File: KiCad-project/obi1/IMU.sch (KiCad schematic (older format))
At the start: 6 parts, among them U6 BMF055

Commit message: Routear
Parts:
- added C42: @1uF;6.3V;X5R;0805;10%, Capacitor_SMD:C_0805_2012Metric_Pad1.18x1.45mm_HandSolder, symbol Device:C
- added R19: @20;1/4W;0805;1%, Resistor_SMD:R_0805_2012Metric_Pad1.20x1.40mm_HandSolder, symbol Device:R
- renumbered C42 to C43, C43 to C44, C44 to C45, R19 to R20
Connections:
- net +3V3: now also C42.1, R19.1
- net GND: now also C42.2
- new net nReset: R19.2
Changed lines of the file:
@@
 	4450 6300 4450 6550
 Wire Wire Line
-	2100 6550 3950 6550
+	2100 6550 2500 6550
 Connection ~ 4250 6550
 Wire Wire Line
 	4250 6550 4350 6550
-Text GLabel 2950 4700 0    50   Input ~ 0
+Text GLabel 2400 4600 0    50   Input ~ 0
 nReset
 $Comp
-L Device:C C42
+L Device:C C43
 U 1 1 605F8DE4
 P 3050 5000
-F 0 "C42" H 3165 5046 50  0000 L CNN
+F 0 "C43" H 3165 5046 50  0000 L CNN
 F 1 "@1uF;6.3V;X5R;0805;10%" H 2550 4900 50  0000 L CNN
 F 2 "Capacitor_SMD:C_0805_2012Metric_Pad1.18x1.45mm_HandSolder" H 3088 4850 50  0001 C CNN
@@
 $EndComp
 Wire Wire Line
-	3550 4800 3050 4800
-Wire Wire Line
 	3050 4800 3050 4850
 Wire Wire Line
@@
 	4350 6550 4450 6550
 $Comp
-L Device:R R19
+L Device:R R20
 U 1 1 605FCDD0
 P 3200 4700
-F 0 "R19" V 2993 4700 50  0000 C CNN
+F 0 "R20" V 2993 4700 50  0000 C CNN
 F 1 "@10K;1/4W;0805;1%" V 3100 4700 50  0000 C CNN
 F 2 "Resistor_SMD:R_0805_2012Metric_Pad1.20x1.40mm_HandSolder" V 3130 4700 50  0001 C CNN
@@
 $EndComp
 Wire Wire Line
-	3350 4700 3550 4700
-Wire Wire Line
 	3050 4700 3000 4700
 Connection ~ 3000 4700
-Wire Wire Line
-	3000 4700 2950 4700
-$Comp
-L Device:C C44
+$Comp
+L Device:C C45
 U 1 1 605FF628
 P 5650 4400
-F 0 "C44" H 5765 4446 50  0000 L CNN
+F 0 "C45" H 5765 4446 50  0000 L CNN
 F 1 "@6800pF;10V;X7R;0603;10%" H 5765 4355 50  0000 L CNN
 F 2 "Capacitor_SMD:C_0603_1608Metric_Pad1.08x0.95mm_HandSolder" H 5688 4250 50  0001 C CNN
@@
 Connection ~ 4450 6550
 $Comp
-L Device:C C43
+L Device:C C44
 U 1 1 606014E1
 P 5200 4400
-F 0 "C43" H 5315 4446 50  0000 L CNN
+F 0 "C44" H 5315 4446 50  0000 L CNN
 F 1 "@0.12uF;10V;X7R;0603;10%" H 4750 4500 50  0000 L CNN
 F 2 "Capacitor_SMD:C_0603_1608Metric_Pad1.08x0.95mm_HandSolder" H 5238 4250 50  0001 C CNN
@@
 	3950 6550 3950 6750
 Connection ~ 3950 6550
-Wire Wire Line
-	3950 6550 4250 6550
+$Comp
+L Device:C C42
+U 1 1 60648C09
+P 2350 5500
+F 0 "C42" H 2465 5546 50  0000 L CNN
+F 1 "@1uF;6.3V;X5R;0805;10%" H 1850 5400 50  0000 L CNN
+F 2 "Capacitor_SMD:C_0805_2012Metric_Pad1.18x1.45mm_HandSolder" H 2388 5350 50  0001 C CNN
+F 3 "~" H 2350 5500 50  0001 C CNN
+	1    2350 5500
+	1    0    0    -1
+$EndComp
+Wire Wire Line
+	2500 6550 2500 5650
+Wire Wire Line
+	2500 5650 2350 5650
+Connection ~ 2500 6550
+Wire Wire Line
+	2500 6550 3950 6550
+Wire Wire Line
+	3550 4800 3050 4800
+Wire Wire Line
+	3350 4700 3550 4700
+$Comp
+L Device:R R19
+U 1 1 60650B61
+P 2600 4600
+F 0 "R19" V 2393 4600 50  0000 C CNN
+F 1 "@20;1/4W;0805;1%" V 2500 4600 50  0000 C CNN
+F 2 "Resistor_SMD:R_0805_2012Metric_Pad1.20x1.40mm_HandSolder" V 2530 4600 50  0001 C CNN
+F 3 "~" H 2600 4600 50  0001 C CNN
+	1    2600 4600
+	0    1    1    0
+$EndComp
+Wire Wire Line
+	2450 4600 2400 4600
+Wire Wire Line
+	2750 4600 2750 4700
+Wire Wire Line
+	2750 5350 2350 5350
+Wire Wire Line
+	2750 4700 3000 4700
+Connection ~ 2750 4700
+Wire Wire Line
+	2750 4700 2750 5350
 $EndSCHEMATC

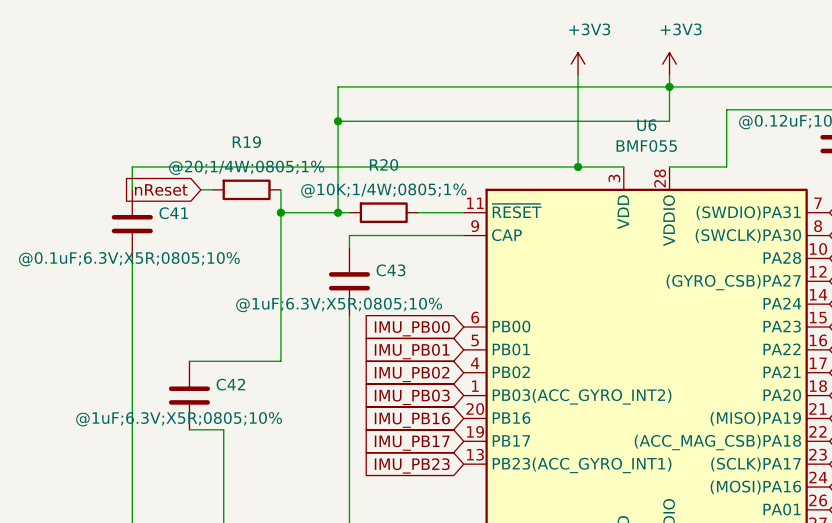
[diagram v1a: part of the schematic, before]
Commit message: Resize board, change layout, re-route IO pins, new imu added
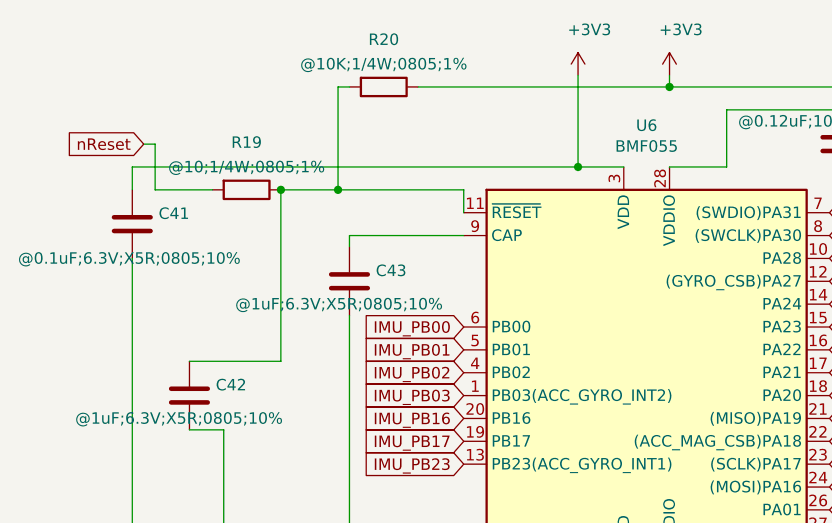
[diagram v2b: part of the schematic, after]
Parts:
- R19: value @20;1/4W;0805;1% -> @10;1/4W;0805;1%
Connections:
- net +3V3: now also R20.1; no longer C42.1, R19.1, R20.2
- net at U6.11 (~RESET): now also C42.1, R19.1, R20.2; no longer R20.1
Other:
- moved on the sheet: R20
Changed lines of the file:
@@
 Wire Wire Line
 	4250 6550 4350 6550
-Text GLabel 2400 4600 0    50   Input ~ 0
+Text GLabel 2150 4400 0    50   Input ~ 0
 nReset
 $Comp
@@
 L Device:R R20
 U 1 1 605FCDD0
-P 3200 4700
-F 0 "R20" V 2993 4700 50  0000 C CNN
-F 1 "@10K;1/4W;0805;1%" V 3100 4700 50  0000 C CNN
-F 2 "Resistor_SMD:R_0805_2012Metric_Pad1.20x1.40mm_HandSolder" V 3130 4700 50  0001 C CNN
-F 3 "~" H 3200 4700 50  0001 C CNN
-	1    3200 4700
+P 3200 4150
+F 0 "R20" V 2993 4150 50  0000 C CNN
+F 1 "@10K;1/4W;0805;1%" V 3100 4150 50  0000 C CNN
+F 2 "Resistor_SMD:R_0805_2012Metric_Pad1.20x1.40mm_HandSolder" V 3130 4150 50  0001 C CNN
+F 3 "~" H 3200 4150 50  0001 C CNN
+	1    3200 4150
 	0    1    1    0
 $EndComp
-Wire Wire Line
-	3050 4700 3000 4700
-Connection ~ 3000 4700
 $Comp
 L Device:C C45
@@
 Connection ~ 5650 4250
 Wire Wire Line
-	4450 4150 3000 4150
+	4450 4150 3350 4150
 Connection ~ 4450 4150
-Wire Wire Line
-	3000 4150 3000 4300
-Wire Wire Line
-	3000 4300 3000 4700
-Connection ~ 3000 4300
-Wire Wire Line
-	4450 4300 3000 4300
-Wire Wire Line
-	4450 4300 4450 4150
 Wire Wire Line
 	4450 4500 4700 4500
@@
 Wire Wire Line
 	3550 4800 3050 4800
-Wire Wire Line
-	3350 4700 3550 4700
 $Comp
 L Device:R R19
@@
 P 2600 4600
 F 0 "R19" V 2393 4600 50  0000 C CNN
-F 1 "@20;1/4W;0805;1%" V 2500 4600 50  0000 C CNN
+F 1 "@10;1/4W;0805;1%" V 2500 4600 50  0000 C CNN
 F 2 "Resistor_SMD:R_0805_2012Metric_Pad1.20x1.40mm_HandSolder" V 2530 4600 50  0001 C CNN
 F 3 "~" H 2600 4600 50  0001 C CNN
@@
 $EndComp
 Wire Wire Line
-	2450 4600 2400 4600
-Wire Wire Line
-	2750 4600 2750 4700
-Wire Wire Line
 	2750 5350 2350 5350
 Wire Wire Line
-	2750 4700 3000 4700
-Connection ~ 2750 4700
+	2200 4600 2200 4400
 Wire Wire Line
-	2750 4700 2750 5350
+	2200 4400 2150 4400
+Wire Wire Line
+	2200 4600 2450 4600
+Wire Wire Line
+	3050 4150 3000 4150
+Wire Wire Line
+	2750 4600 2750 5350
+Wire Wire Line
+	3550 4600 3550 4700
+Connection ~ 2750 4600
+Wire Wire Line
+	3000 4150 3000 4600
+Wire Wire Line
+	2750 4600 3000 4600
+Connection ~ 3000 4600
+Wire Wire Line
+	3000 4600 3550 4600
 $EndSCHEMATC

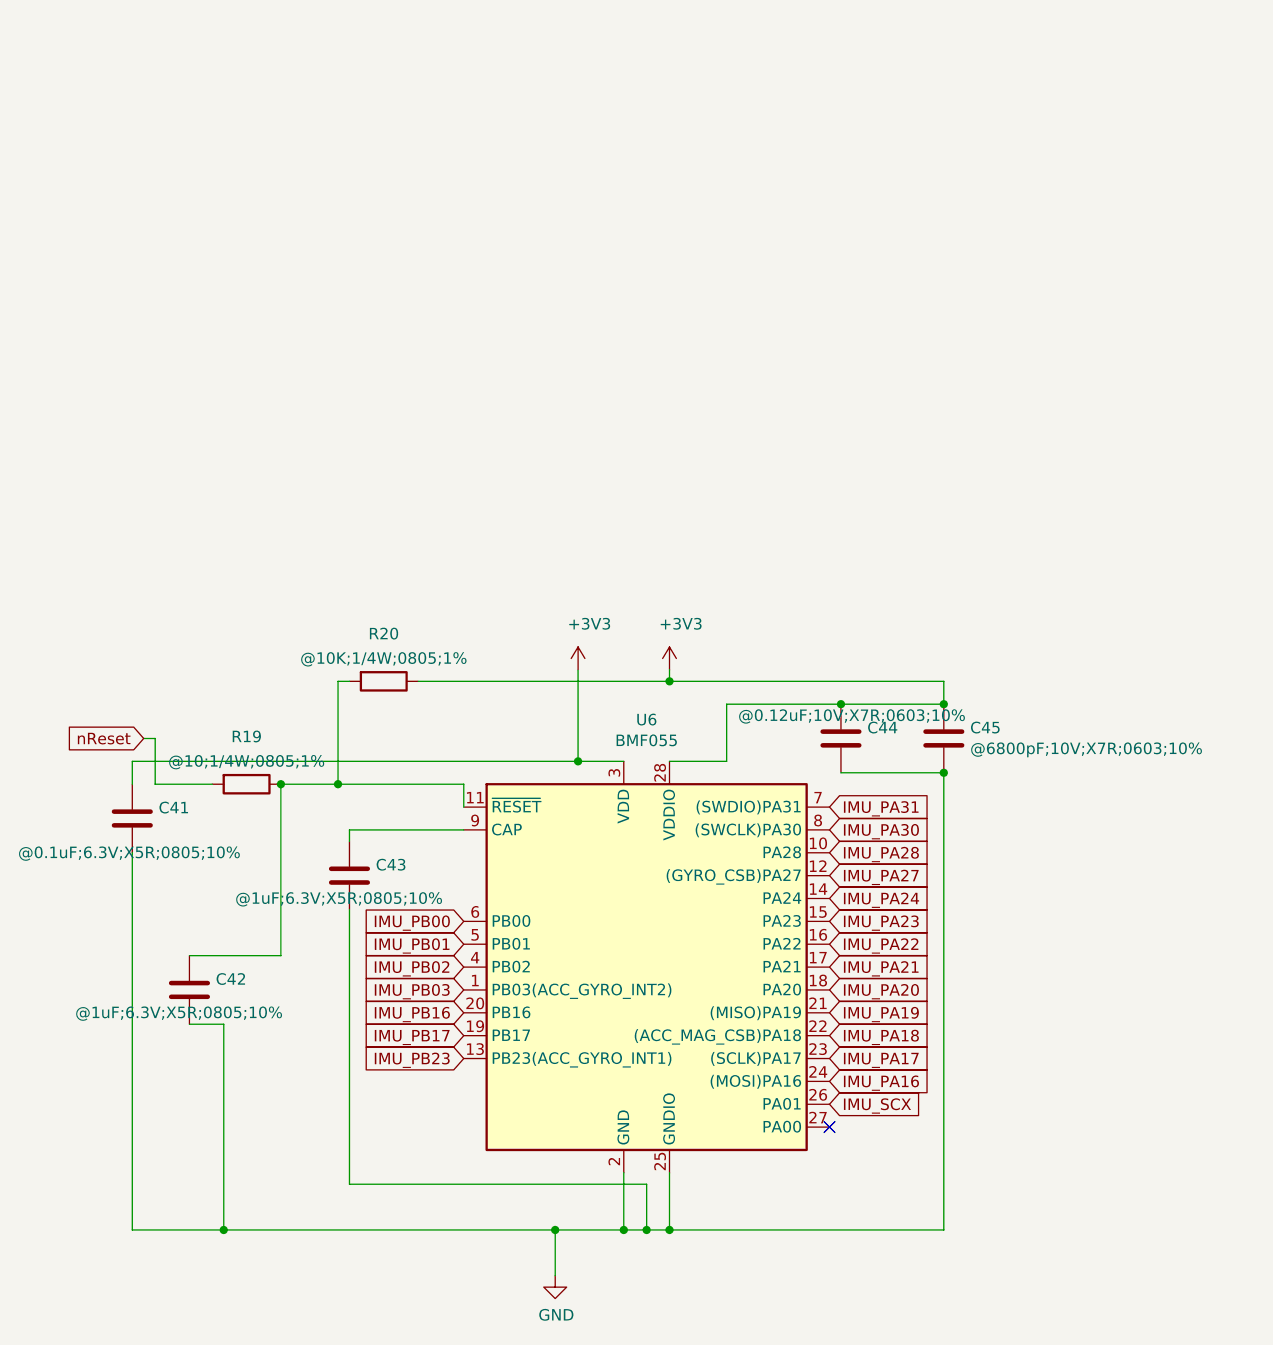
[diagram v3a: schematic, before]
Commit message: IMU changed again, Final IMU= LSM6DSMTR, First Order to OSHPark
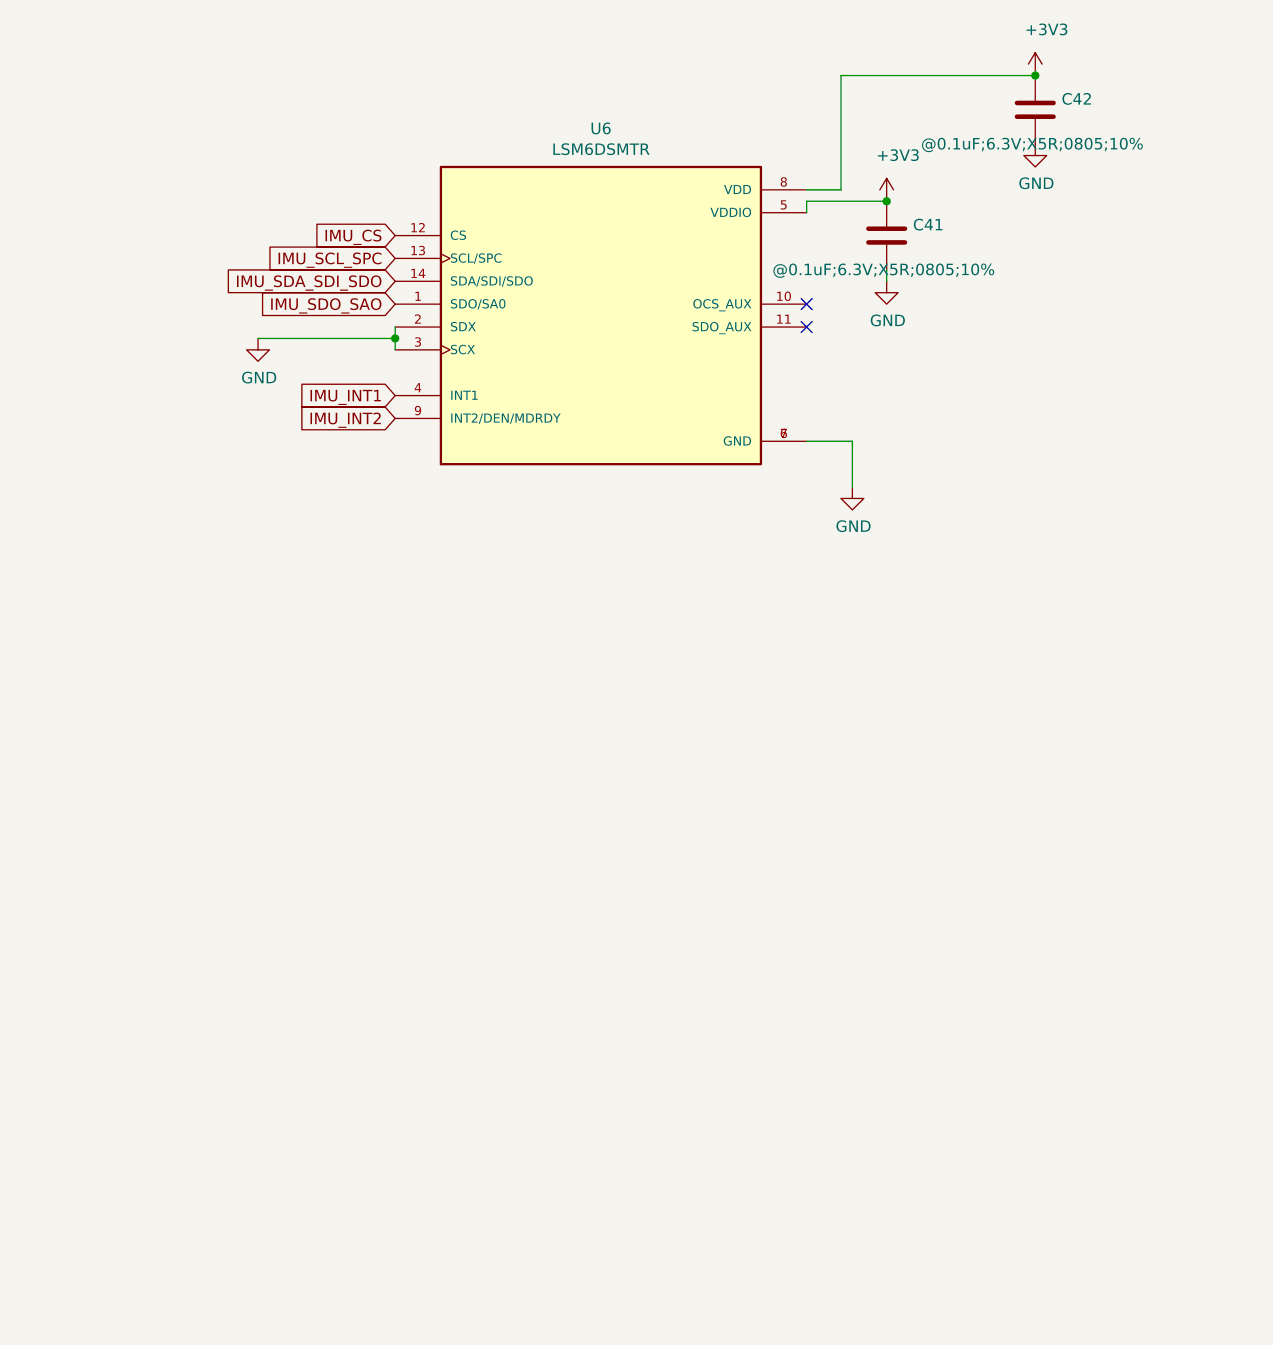
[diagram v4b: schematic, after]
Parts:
- removed C43: @1uF;6.3V;X5R;0805;10%, Capacitor_SMD:C_0805_2012Metric_Pad1.18x1.45mm_HandSolder, symbol Device:C
- removed C44: @0.12uF;10V;X7R;0603;10%, Capacitor_SMD:C_0603_1608Metric_Pad1.08x0.95mm_HandSolder, symbol Device:C
- removed C45: @6800pF;10V;X7R;0603;10%, Capacitor_SMD:C_0603_1608Metric_Pad1.08x0.95mm_HandSolder, symbol Device:C
- removed R19: @10;1/4W;0805;1%, Resistor_SMD:R_0805_2012Metric_Pad1.20x1.40mm_HandSolder, symbol Device:R
- removed R20: @10K;1/4W;0805;1%, Resistor_SMD:R_0805_2012Metric_Pad1.20x1.40mm_HandSolder, symbol Device:R
- removed U6: BMF055, Package_LGA:LGA-28_5.2x3.8mm_P0.5mm, symbol Sensor_Motion:BMF055
- added U6: LSM6DSMTR, PQFN50P300X250X86-14N, symbol egalan:LSM6DSMTR
- C42: value @1uF;6.3V;X5R;0805;10% -> @0.1uF;6.3V;X5R;0805;10%
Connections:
- net +3V3: now also C42.1, U6.5 (VDDIO), U6.8 (VDD)
- net GND: now also U6.2 (SDX), U6.3 (SCX), U6.6 (GND), U6.7 (GND)
- new net IMU_CS: U6.12 (CS)
- new net IMU_INT1: U6.4 (INT1)
- new net IMU_INT2: U6.9 (INT2/DEN/MDRDY)
- new net IMU_SCL_SPC: U6.13 (SCL/SPC)
- new net IMU_SDA_SDI_SDO: U6.14 (SDA/SDI/SDO)
- new net IMU_SDO_SAO: U6.1 (SDO/SA0)
- no-connect marks 1 -> 2
